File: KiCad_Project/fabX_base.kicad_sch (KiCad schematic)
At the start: 39 parts, among them J1 SolderJumper_2_Open, J2 SolderJumper_2_Open, J3 SolderJumper_2_Open, J4 SolderJumper_2_Open, J5 SolderJumper_2_Open, J6 SolderJumper_2_Open, Q5 BCX19, Q6 BCX19, U1 MCP23008, U2 MCP23008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

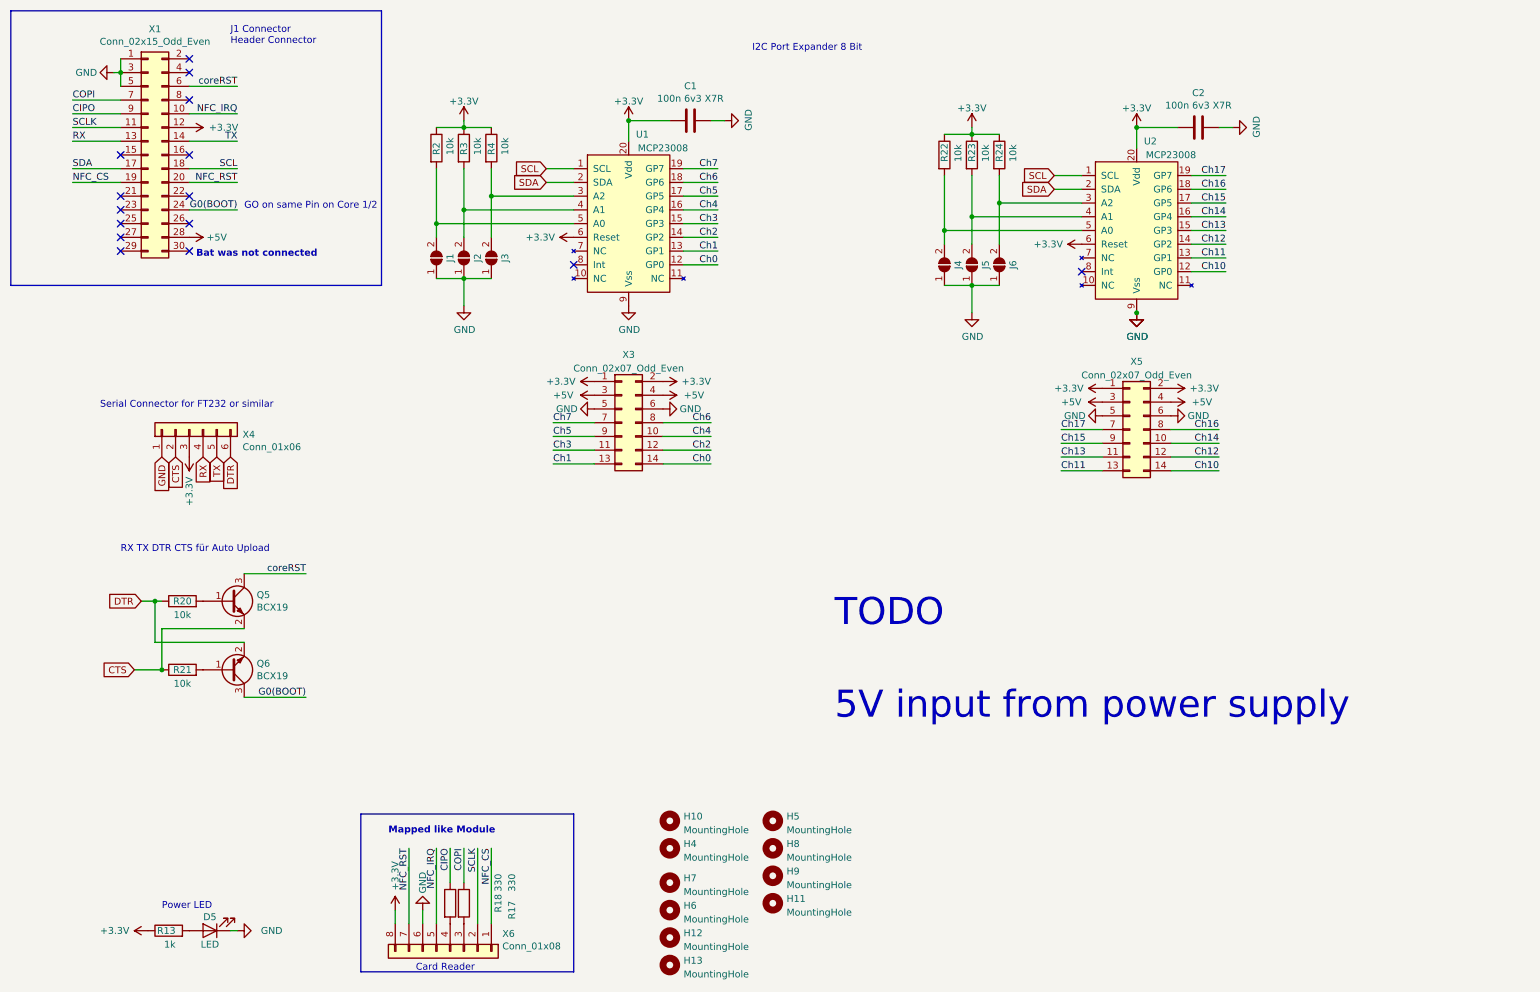
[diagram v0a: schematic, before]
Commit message: add pulldowns to inputs
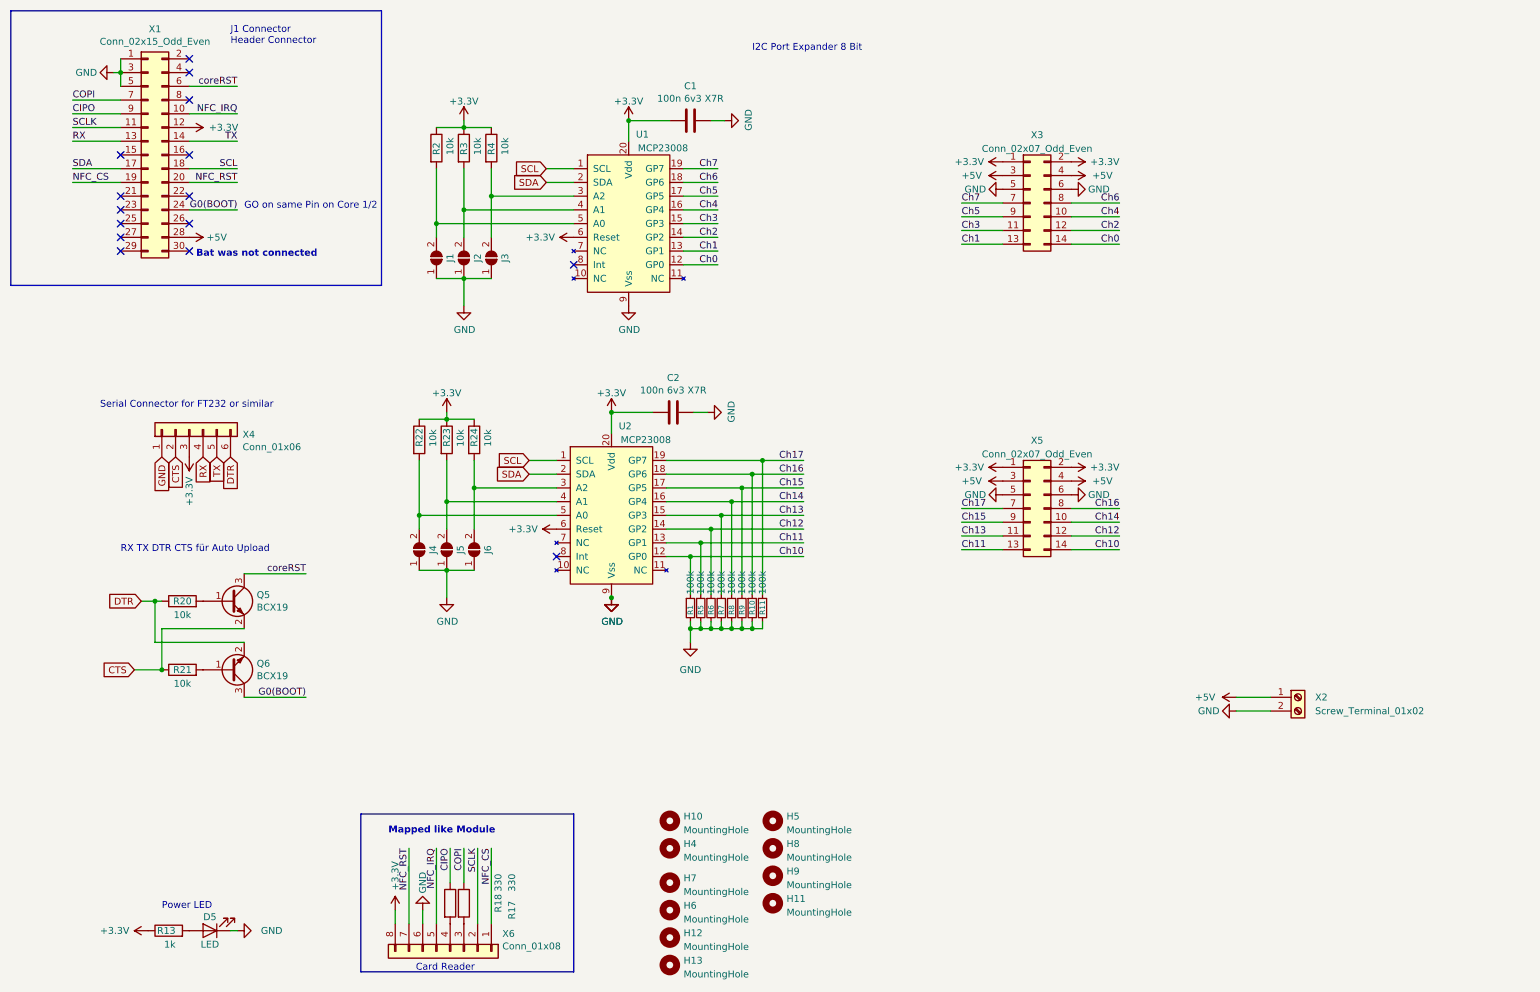
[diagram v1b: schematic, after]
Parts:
- added R1, R10, R11, R5, R6, R7, R8, R9: 100k, symbol Device:R_Small
- added X2: Screw_Terminal_01x02, Connector_Phoenix_MSTB:PhoenixContact_MSTBA_2,5_2-G-5,08_1x02_P5.08mm_Horizontal, symbol Connector:Screw_Terminal_01x02
- D5: footprint ownLEDs:LED_1206_3216Metric_ReverseMount_Hole1.8x2.4mm_3DMOD -> LED_SMD:LED_0603_1608Metric
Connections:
- net +5V: now also X2.1 (Pin_1)
- net Ch10: now also R1.1
- net Ch11: now also R5.1
- net Ch12: now also R6.1
- net Ch13: now also R7.1
- net Ch14: now also R8.1
- net Ch15: now also R9.1
- net Ch16: now also R10.1
- net Ch17: now also R11.1
- net GND: now also R1.2, R10.2, R11.2, R5.2, R6.2, R7.2, R8.2, R9.2, X2.2 (Pin_2)
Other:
- note removed: "5V input from power supply"
- note removed: "TODO"
- moved on the sheet: C2, J4, J5, J6, R22, R23, R24, U2, X3, X5

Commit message: place pulldowns
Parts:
- R1, R10, R11, R5, R6, R7, R8, R9: footprint (none) -> Resistor_SMD:R_0603_1608Metric
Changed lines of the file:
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@@
       (effects (font (size 1.27 1.27)) (justify left))
     )
-    (property "Footprint" "" (at 155.575 125.73 0)
+    (property "Footprint" "Resistor_SMD:R_0603_1608Metric" (at 155.575 125.73 0)
       (effects (font (size 1.27 1.27)) hide)
     )
@@
       (effects (font (size 1.27 1.27)) (justify left))
     )
-    (property "Footprint" "" (at 151.765 125.73 0)
+    (property "Footprint" "Resistor_SMD:R_0603_1608Metric" (at 151.765 125.73 0)
       (effects (font (size 1.27 1.27)) hide)
     )
@@
       (effects (font (size 1.27 1.27)) (justify left))
     )
-    (property "Footprint" "" (at 147.955 125.73 0)
+    (property "Footprint" "Resistor_SMD:R_0603_1608Metric" (at 147.955 125.73 0)
       (effects (font (size 1.27 1.27)) hide)
     )
@@
       (effects (font (size 1.27 1.27)) (justify left))
     )
-    (property "Footprint" "" (at 153.67 125.73 0)
+    (property "Footprint" "Resistor_SMD:R_0603_1608Metric" (at 153.67 125.73 0)
       (effects (font (size 1.27 1.27)) hide)
     )
@@
       (effects (font (size 1.27 1.27)) (justify left))
     )
-    (property "Footprint" "" (at 149.86 125.73 0)
+    (property "Footprint" "Resistor_SMD:R_0603_1608Metric" (at 149.86 125.73 0)
       (effects (font (size 1.27 1.27)) hide)
     )
@@
       (effects (font (size 1.27 1.27)) (justify left))
     )
-    (property "Footprint" "" (at 146.05 125.73 0)
+    (property "Footprint" "Resistor_SMD:R_0603_1608Metric" (at 146.05 125.73 0)
       (effects (font (size 1.27 1.27)) hide)
     )
@@
       (effects (font (size 1.27 1.27)) (justify left))
     )
-    (property "Footprint" "" (at 144.145 125.73 0)
+    (property "Footprint" "Resistor_SMD:R_0603_1608Metric" (at 144.145 125.73 0)
       (effects (font (size 1.27 1.27)) hide)
     )
@@
       (effects (font (size 1.27 1.27)) (justify left))
     )
-    (property "Footprint" "" (at 142.24 125.73 0)
-      (effects (font (size 1.27 1.27)) hide)
-    )
+    (property "Footprint" "Resistor_SMD:R_0603_1608Metric" (at 142.24 125.73 0)
+      (effects (font (size 1.27 1.27)) hide)
+    )
